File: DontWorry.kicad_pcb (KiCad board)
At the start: 2 copper layers, 71 x 54 mm, 25 parts, among them J1 Conn_02x03_Odd_Even, J2 Conn_02x03_Odd_Even, J3 Conn_01x14, Q5 BC849, Q6 BC849, Q7 BC849, Q8 BC849, Q9 BC849

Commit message: Updated PCB
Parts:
- removed J3: Conn_01x14, Connector_PinHeader_2.54mm:PinHeader_2x07_P2.54mm_Vertical
- added J4: Conn_01x06, Connector_PinHeader_2.54mm:PinHeader_2x03_P2.54mm_Vertical, F.Cu at (120.1, 83.1)
- added R14: 10K, Resistor_SMD:R_0805_2012Metric, F.Cu at (134.6, 66.6)
- added R15: 10K, Resistor_SMD:R_0805_2012Metric, F.Cu at (134.6, 64.1)
- added R16: 10K, Resistor_SMD:R_0805_2012Metric, F.Cu at (134.6, 61.5)
- added R17: 10K, Resistor_SMD:R_0805_2012Metric, F.Cu at (122.5, 64.1)
- added R18: 10K, Resistor_SMD:R_0805_2012Metric, F.Cu at (122.5, 66.6)
- 7-SEG DISPLAY CC: renamed from 7SEG-DISPLAY CC
- H4 (GND): renamed from H4
- J1, J2: footprint Connector_IDC:IDC-Header_2x03_P2.54mm_Vertical -> Connector_PinHeader_2.54mm:PinHeader_2x03_P2.54mm_Vertical
- moved J1 5.46 mm to (129.5, 66.5), turned to 180 degrees
- moved J2 4.94 mm to (179.9, 66.5), turned to 180 degrees
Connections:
- J1 pad 1: unconnected-(J1-Pin_1-Pad1) -> /A1
- J1 pad 2: unconnected-(J1-Pin_2-Pad2) -> /A4
- J1 pad 3: unconnected-(J1-Pin_3-Pad3) -> /A2
- J1 pad 4: unconnected-(J1-Pin_4-Pad4) -> /A5
- J1 pad 5: unconnected-(J1-Pin_5-Pad5) -> /A3
- J2 pad 1: unconnected-(J2-Pin_1-Pad1) -> +5V
- J2 pad 2: unconnected-(J2-Pin_2-Pad2) -> +5V
- J2 pad 3: unconnected-(J2-Pin_3-Pad3) -> +5V
- J2 pad 4: unconnected-(J2-Pin_4-Pad4) -> +5V
- J2 pad 5: unconnected-(J2-Pin_5-Pad5) -> +5V
- J2 pad 6: unconnected-(J2-Pin_6-Pad6) -> +5V
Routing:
- net +3.3V: track 48.7 -> 0.00 mm
- net +5V: track 53.2 -> 73.7 mm
- net /A1: track 28.4 -> 15.2 mm
- net /A2: track 22.7 -> 13.6 mm
- net /A3: track 23.2 -> 16.6 mm
- net /A5: track 17.4 -> 11.0 mm
- net GND: track 129.0 -> 133.8 mm
- net /A4: track 17.6 -> 14.9 mm
- net Net-(U1-g): track 21.8 -> 21.9 mm, vias 2 -> 1
- added copper zone on B.Cu, net +5V
- added copper zone on F.Cu, net +5V
- added copper zone on F.Cu, net GND
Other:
- board text added: "-/A3"
- board text added: "A4/A1"
- board text added: "A5/A2"
- board text added: "DontWorry_0.1"
- board text added: "GND/5V"
- board text added: "{dblquote}Don't Worry{dblquote} PCB V_0.1"
- board text removed: "A1/GND"
- board text removed: "A3/A2"
- board text removed: "A5/A4"
- board text removed: "X/3.3V"
- board text removed: "X/5V"

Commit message: Added bottom GND fill
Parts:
- moved H4 (GND) 6.08 mm to (183.0, 103.0)
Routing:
- net GND: track 133.8 -> 130.3 mm
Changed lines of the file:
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@@
 		(tags "resistor")
 		(property "Reference" "R15"
-			(at 3 0 360)
+			(at 3 0 0)
 			(layer "F.SilkS")
 			(effects
@@
 		)
 		(property "Value" "10K"
-			(at 0 1.65 360)
+			(at 0 1.65 0)
 			(layer "F.Fab")
 			(effects
@@
 		)
 		(fp_text user "${REFERENCE}"
-			(at 0 0 360)
+			(at 0 0 0)
 			(layer "F.Fab")
 			(effects
@@
 		(tags "resistor")
 		(property "Reference" "R14"
-			(at 3 0 360)
+			(at 3 0 0)
 			(layer "F.SilkS")
 			(effects
@@
 		)
 		(property "Value" "10K"
-			(at 0 1.65 360)
+			(at 0 1.65 0)
 			(layer "F.Fab")
 			(effects
@@
 		)
 		(fp_text user "${REFERENCE}"
-			(at 0 0 360)
+			(at 0 0 0)
 			(layer "F.Fab")
 			(effects
@@
 		(tags "resistor")
 		(property "Reference" "R16"
-			(at 3 0 360)
+			(at 3 0 0)
 			(layer "F.SilkS")
 			(effects
@@
 		)
 		(property "Value" "10K"
-			(at 0 1.65 360)
+			(at 0 1.65 0)
 			(layer "F.Fab")
 			(effects
@@
 		)
 		(fp_text user "${REFERENCE}"
-			(at 0 0 360)
+			(at 0 0 0)
 			(layer "F.Fab")
 			(effects
@@
 		)
 		(property "Value" "BC849"
-			(at -2.7155 3.7694 180)
+			(at -0.0351 2.9826 -90)
 			(layer "F.SilkS")
 			(effects
@@
 	(footprint "MountingHole:MountingHole_3.2mm_M3_DIN965_Pad"
 		(layer "F.Cu")
-		(at 182 97)
+		(at 183 103)
 		(descr "Mounting Hole 3.2mm, M3, DIN965")
 		(tags "mounting hole 3.2mm m3 din965")
 		(property "Reference" "H4 (GND)"
-			(at 0 4.6 0)
+			(at -0.2 -4.1 0)
 			(layer "F.SilkS")
 			(effects
@@
 		)
 	)
+	(gr_circle
+		(center 183 102.9)
+		(end 188 102.9)
+		(stroke
+			(width 0.2)
+			(type solid)
+		)
+		(fill solid)
+		(layer "B.Cu")
+		(net 4)
+	)
 	(gr_rect
 		(start 151 76)
@@
 	)
 	(segment
-		(start 170.9784 102.5)
-		(end 180.7 102.5)
+		(start 173.2026 83.7946)
+		(end 173.2026 94.4372)
 		(width 0.75)
 		(layer "F.Cu")
@@
 	)
 	(segment
-		(start 173.2026 83.7946)
-		(end 173.2026 94.4372)
+		(start 172.2374 95.4024)
+		(end 170.9674 95.4024)
 		(width 0.75)
 		(layer "F.Cu")
@@
 	)
 	(segment
-		(start 172.2374 95.4024)
-		(end 170.9674 95.4024)
+		(start 179.5 103.1)
+		(end 182.9 103.1)
 		(width 0.75)
 		(layer "F.Cu")
@@
 	)
 	(segment
+		(start 178.889 102.489)
+		(end 179.5 103.1)
+		(width 0.75)
+		(layer "F.Cu")
+		(net 4)
+	)
+	(segment
 		(start 172.1612 82.7532)
 		(end 171.1631 81.7551)
@@
 	)
 	(segment
-		(start 180.7 102.5)
-		(end 182 101.2)
+		(start 170.9674 102.489)
+		(end 178.889 102.489)
 		(width 0.75)
 		(layer "F.Cu")
@@
 	)
 	(segment
-		(start 182 101.2)
-		(end 182 97)
+		(start 154.3304 81.7551)
+		(end 160.19925 81.7551)
 		(width 0.75)
 		(layer "F.Cu")
@@
 	)
 	(segment
-		(start 154.3304 81.7551)
-		(end 160.19925 81.7551)
+		(start 163.1 73.7)
+		(end 163.1 69.3375)
 		(width 0.75)
 		(layer "F.Cu")
@@
 	)
 	(segment
-		(start 163.1 73.7)
-		(end 163.1 69.3375)
+		(start 182.9 103.1)
+		(end 183 103)
 		(width 0.75)
 		(layer "F.Cu")
@@
 		(polygon
 			(pts
-				(xy 191 52) (xy 115 52) (xy 115 115) (xy 191 115)
+				(xy 191 89.4) (xy 191 52) (xy 115 52) (xy 115 115) (xy 174.4 115) (xy 191 115)
 			)
 		)

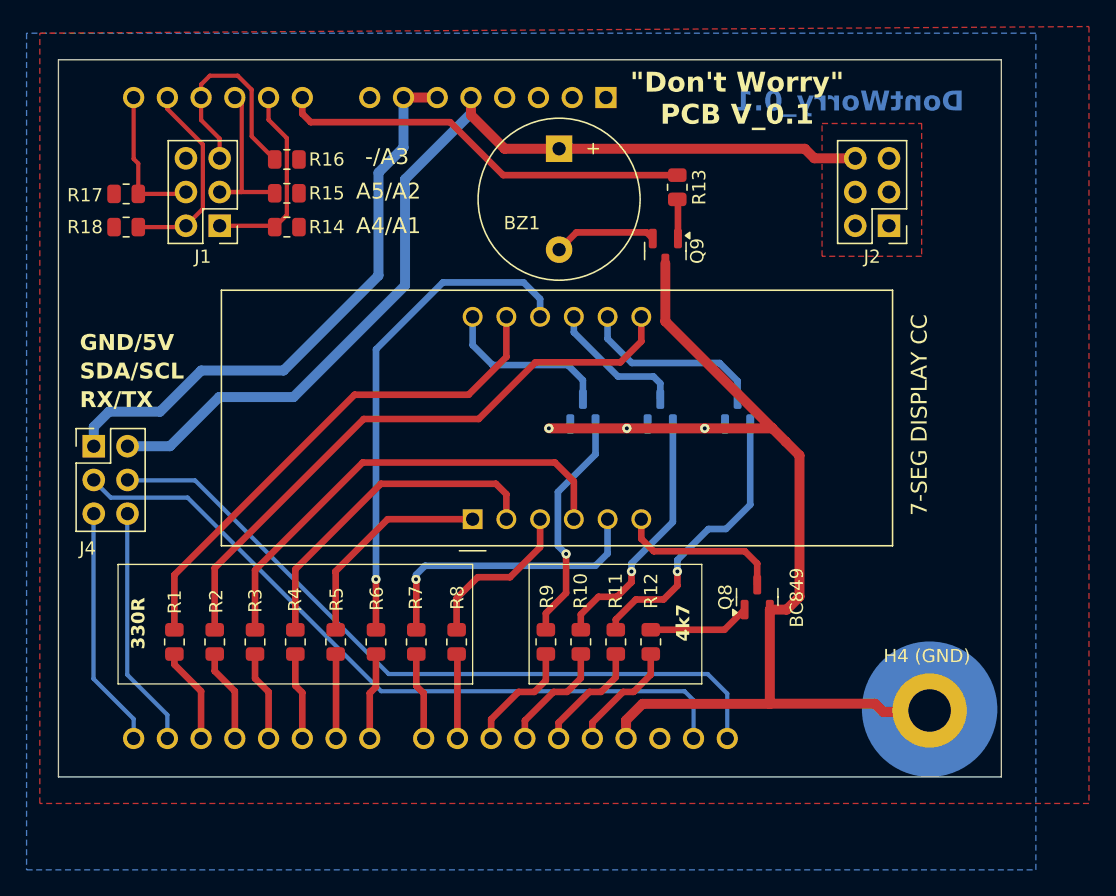
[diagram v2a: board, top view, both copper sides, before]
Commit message: Added more descriptions on Silk
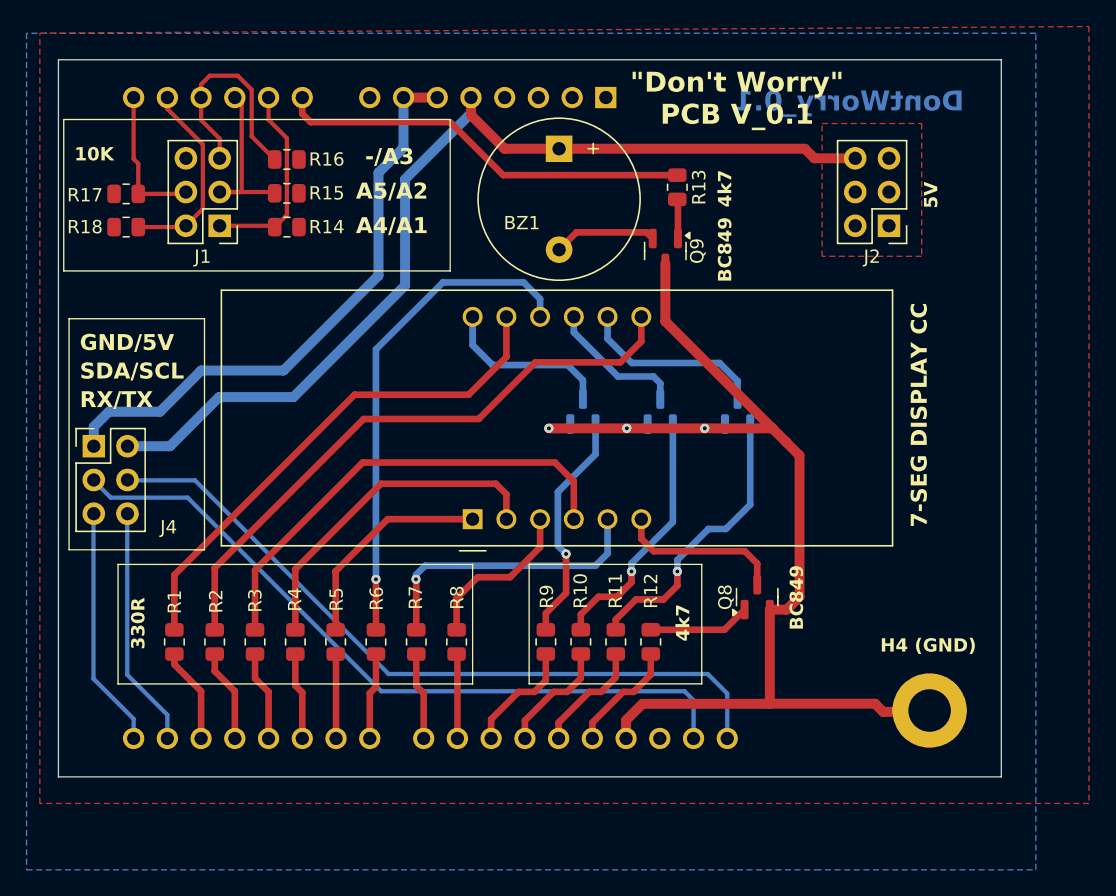
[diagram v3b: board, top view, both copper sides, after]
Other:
- board text added: "10K"
- board text added: "4k7"
- board text added: "5V"
- board text added: "BC849"
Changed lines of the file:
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@@
 				(font
 					(size 1.2 1.2)
-					(thickness 0.15)
+					(thickness 0.2)
+					(bold yes)
 				)
 			)
@@
 		(tags "Through hole pin header THT 2x03 2.54mm double row")
 		(property "Reference" "J4"
-			(at -0.46 7.7 0)
+			(at 5.64 6.1 0)
 			(layer "F.SilkS")
 			(effects
@@
 		)
 		(property "Value" "BC849"
-			(at -0.0351 2.9826 -90)
-			(layer "F.SilkS")
+			(at -0.0351 2.9826 270)
+			(layer "F.SilkS" knockout)
 			(effects
 				(font
 					(size 1 1)
-					(thickness 0.15)
+					(thickness 0.2)
+					(bold yes)
 				)
 			)
@@
 		(tags "mounting hole 3.2mm m3 din965")
 		(property "Reference" "H4 (GND)"
-			(at -0.2 -4.1 0)
-			(layer "F.SilkS")
+			(at -0.1 -4.9 0)
+			(layer "F.SilkS" knockout)
 			(effects
 				(font
 					(size 1 1)
-					(thickness 0.15)
+					(thickness 0.2)
+					(bold yes)
 				)
 			)
@@
 		)
 	)
-	(gr_circle
-		(center 183 102.9)
-		(end 188 102.9)
-		(stroke
-			(width 0.2)
-			(type solid)
-		)
-		(fill solid)
-		(layer "B.Cu")
-		(net 4)
-	)
 	(gr_rect
 		(start 151 76)
@@
 	)
 	(gr_rect
+		(start 118.2 73.5)
+		(end 128.4 90.9)
+		(stroke
+			(width 0.1)
+			(type default)
+		)
+		(fill none)
+		(layer "F.SilkS")
+	)
+	(gr_rect
 		(start 152.8438 91.9958)
 		(end 165.8438 100.9958)
@@
 		(layer "F.SilkS")
 	)
+	(gr_rect
+		(start 117.8 58.5)
+		(end 146.9 69.9)
+		(stroke
+			(width 0.1)
+			(type default)
+		)
+		(fill none)
+		(layer "F.SilkS")
+	)
 	(gr_line
 		(start 188.4 54)
@@
 			(font
 				(size 1.2 1.2)
-				(thickness 0.15)
+				(thickness 0.2)
+				(bold yes)
 			)
 			(justify left bottom)
@@
 			(font
 				(size 1.2 1.2)
-				(thickness 0.15)
+				(thickness 0.2)
 				(bold yes)
 			)
@@
 			(font
 				(size 1.2 1.2)
-				(thickness 0.15)
+				(thickness 0.2)
+				(bold yes)
 			)
 			(justify left bottom)
 		)
 	)
+	(gr_text "10K"
+		(at 118.6 61.7 0)
+		(layer "F.SilkS" knockout)
+		(effects
+			(font
+				(size 1 1)
+				(thickness 0.2)
+				(bold yes)
+			)
+			(justify left bottom)
+		)
+	)
+	(gr_text "BC849"
+		(at 167.6 68.3 90)
+		(layer "F.SilkS" knockout)
+		(effects
+			(font
+				(size 1 1)
+				(thickness 0.2)
+				(bold yes)
+			)
+		)
+	)
 	(gr_text "{dblquote}Don't Worry{dblquote} \nPCB V_0.1"
 		(at 168.5 59 0)
@@
 		)
 	)
+	(gr_text "5V"
+		(at 183.7 65.2 90)
+		(layer "F.SilkS" knockout)
+		(effects
+			(font
+				(size 1 1)
+				(thickness 0.2)
+				(bold yes)
+			)
+			(justify left bottom)
+		)
+	)
 	(gr_text "RX/TX"
 		(at 119 80.3 0)
@@
 			(font
 				(size 1.2 1.2)
-				(thickness 0.15)
+				(thickness 0.2)
 				(bold yes)
 			)
@@
 			(font
 				(size 1.2 1.2)
-				(thickness 0.15)
+				(thickness 0.2)
 				(bold yes)
 			)
@@
 		)
 	)
+	(gr_text "4k7"
+		(at 167.6 63.7 90)
+		(layer "F.SilkS" knockout)
+		(effects
+			(font
+				(size 1 1)
+				(thickness 0.2)
+				(bold yes)
+			)
+		)
+	)
 	(gr_text "A5/A2"
 		(at 139.8 64.6 0)
@@
 			(font
 				(size 1.2 1.2)
-				(thickness 0.15)
+				(thickness 0.2)
+				(bold yes)
 			)
 			(justify left bottom)

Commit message: Updated traces and Silk style
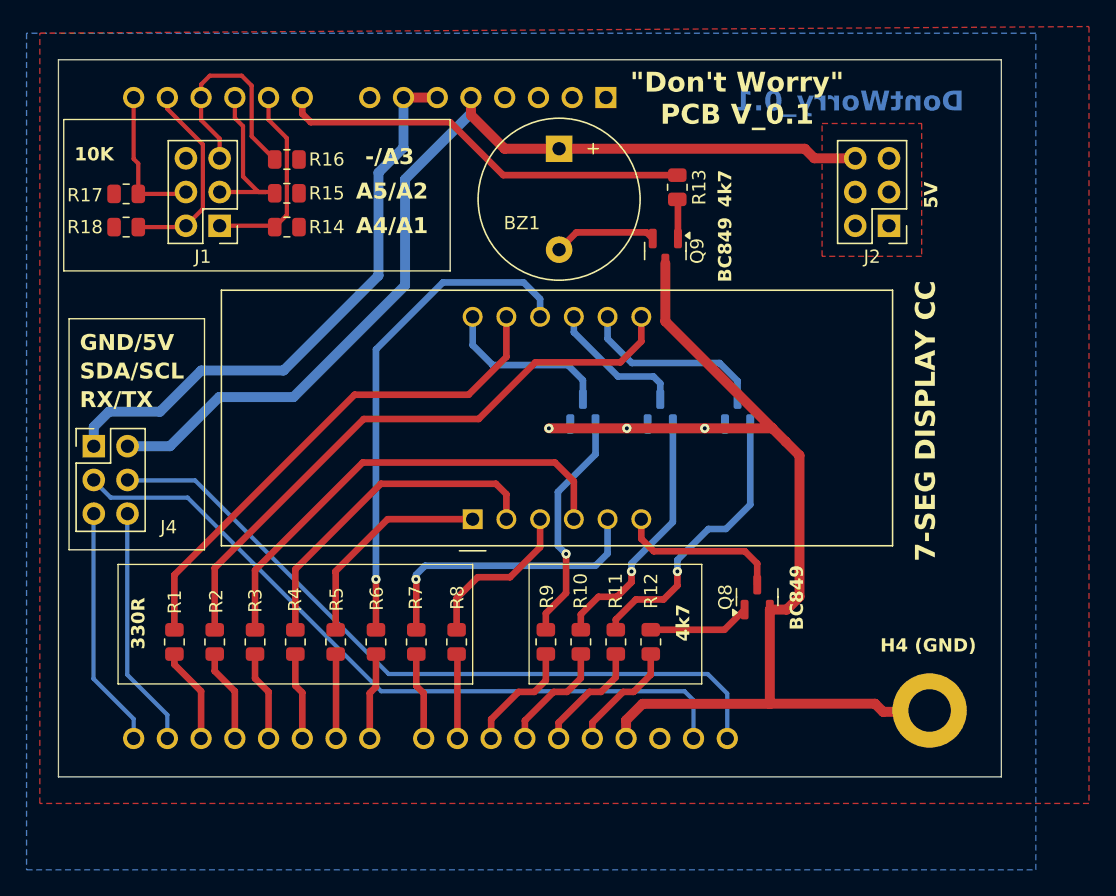
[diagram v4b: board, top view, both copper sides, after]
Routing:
- net /A2: track 13.6 -> 13.0 mm
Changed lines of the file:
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@@
 		(tags "4 digit 7 segment green LED")
 		(property "Reference" "7-SEG DISPLAY CC"
-			(at 7.8452 33.635 90)
+			(at 7.3952 34.11 90)
 			(layer "F.SilkS" knockout)
 			(effects
 				(font
-					(size 1.2 1.2)
-					(thickness 0.2)
+					(size 1.5 1.5)
+					(thickness 0.3)
 					(bold yes)
 				)
@@
 		)
 		(property "Value" "BC849"
-			(at -0.0351 2.9826 270)
+			(at -0.0351 2.9826 -90)
 			(layer "F.SilkS" knockout)
 			(effects
@@
 			(font
 				(size 1.2 1.2)
-				(thickness 0.2)
+				(thickness 0.25)
 				(bold yes)
 			)
@@
 			(font
 				(size 1.2 1.2)
-				(thickness 0.2)
+				(thickness 0.25)
 				(bold yes)
 			)
@@
 			(font
 				(size 1.2 1.2)
-				(thickness 0.2)
+				(thickness 0.25)
 				(bold yes)
 			)
@@
 			(font
 				(size 1.2 1.2)
-				(thickness 0.2)
+				(thickness 0.25)
 				(bold yes)
 			)
@@
 			(font
 				(size 1.2 1.2)
-				(thickness 0.2)
+				(thickness 0.25)
 				(bold yes)
 			)
@@
 			(font
 				(size 1.2 1.2)
-				(thickness 0.2)
+				(thickness 0.25)
 				(bold yes)
 			)
@@
 	)
 	(segment
-		(start 128.143 56.8452)
-		(end 128.143 55.857)
+		(start 131.95 59.771333)
+		(end 133.6875 61.508833)
 		(width 0.32)
 		(layer "F.Cu")
@@
 	)
 	(segment
-		(start 130.9 55.2)
-		(end 131.95 56.25)
+		(start 131.95 55.95)
+		(end 131.95 59.771333)
 		(width 0.32)
 		(layer "F.Cu")
@@
 	)
 	(segment
-		(start 131.95 59.771333)
-		(end 133.6875 61.508833)
+		(start 128.143 58.543)
+		(end 129.54 59.94)
 		(width 0.32)
 		(layer "F.Cu")
@@
 	)
 	(segment
-		(start 128.8 55.2)
-		(end 130.9 55.2)
+		(start 131.2 55.2)
+		(end 131.95 55.95)
 		(width 0.32)
 		(layer "F.Cu")
@@
 	)
 	(segment
-		(start 131.95 56.25)
-		(end 131.95 59.771333)
+		(start 129.54 59.94)
+		(end 129.54 61.42)
 		(width 0.32)
 		(layer "F.Cu")
@@
 	)
 	(segment
-		(start 128.143 58.543)
-		(end 129.54 59.94)
+		(start 128.143 56.8452)
+		(end 128.143 58.543)
 		(width 0.32)
 		(layer "F.Cu")
@@
 	)
 	(segment
-		(start 129.54 59.94)
-		(end 129.54 61.42)
+		(start 128.8 55.2)
+		(end 131.2 55.2)
 		(width 0.32)
 		(layer "F.Cu")
@@
 	(segment
 		(start 128.143 56.8452)
-		(end 128.143 58.543)
+		(end 128.143 55.857)
 		(width 0.32)
 		(layer "F.Cu")
@@
 	)
 	(segment
-		(start 131.2 57.3622)
-		(end 130.683 56.8452)
+		(start 131.3 62.8)
+		(end 132.46 63.96)
 		(width 0.32)
 		(layer "F.Cu")
@@
 	)
 	(segment
-		(start 131.2 63.96)
-		(end 131.2 57.3622)
+		(start 131.3 59)
+		(end 131.3 62.8)
 		(width 0.32)
 		(layer "F.Cu")
@@
 	)
 	(segment
-		(start 129.54 63.96)
-		(end 131.2 63.96)
+		(start 133 63.96)
+		(end 133.593084 63.96)
 		(width 0.32)
 		(layer "F.Cu")
@@
 	(segment
 		(start 129.54 63.96)
-		(end 133.593084 63.96)
+		(end 133 63.96)
+		(width 0.32)
+		(layer "F.Cu")
+		(net 45)
+	)
+	(segment
+		(start 130.683 58.383)
+		(end 131.3 59)
+		(width 0.32)
+		(layer "F.Cu")
+		(net 45)
+	)
+	(segment
+		(start 132.46 63.96)
+		(end 133 63.96)
+		(width 0.32)
+		(layer "F.Cu")
+		(net 45)
+	)
+	(segment
+		(start 130.683 56.8452)
+		(end 130.683 58.383)
 		(width 0.32)
 		(layer "F.Cu")
